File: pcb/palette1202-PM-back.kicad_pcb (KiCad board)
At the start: 2 copper layers, 100 x 86.8 mm, 9 parts

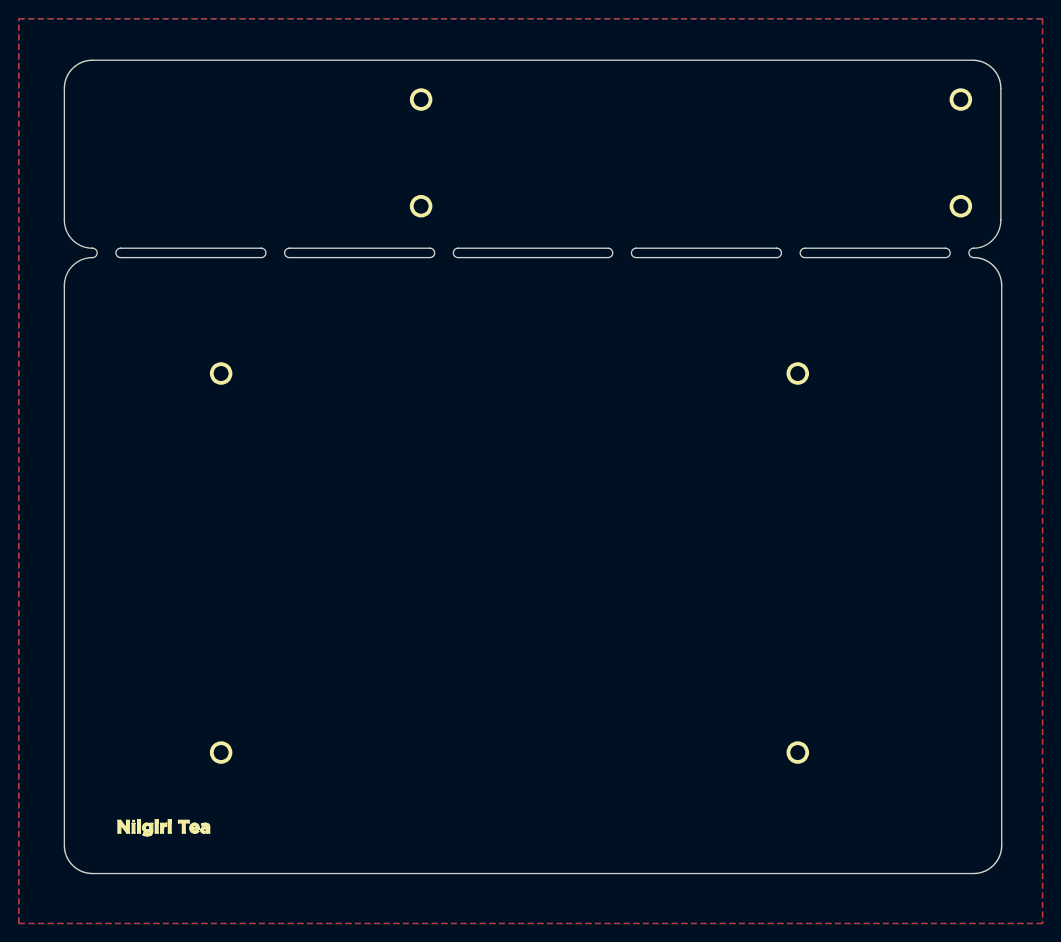
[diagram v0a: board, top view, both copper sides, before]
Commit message: updated back panel
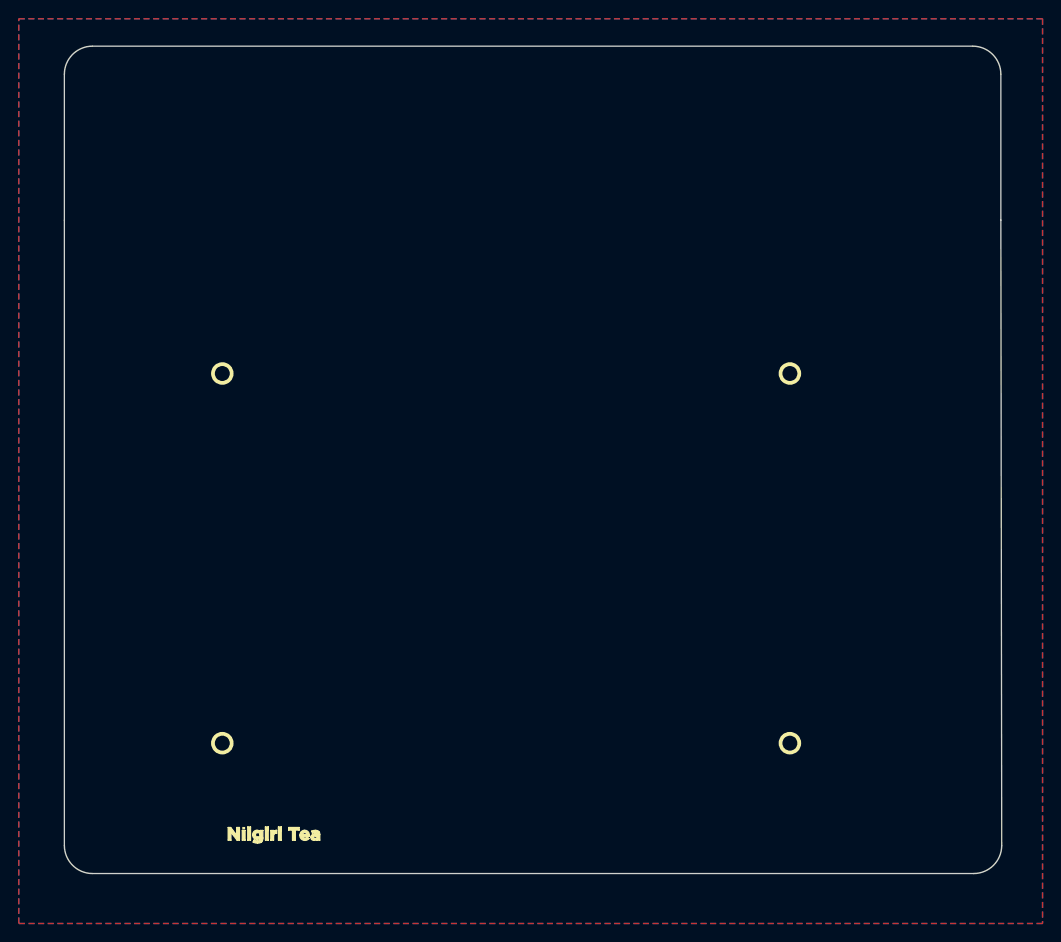
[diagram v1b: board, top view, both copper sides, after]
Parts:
- removed H1, H2, H3, H4: MountingHole, nilgiri:M2_vis
- removed the H99 at (95.1, 119.4)
- added H99: MountingHole, nilgiri:nil_logo, F.Cu at (106.8, 120.1)
- added H99: MountingHole, nilgiri:nil_logo, B.Cu at (108.3, 120.1)
- moved H8 1.31 mm to (163.5, 110.3)
- moved H6 1.01 mm to (103.0, 110.3)
- moved H7 0.84 mm to (163.5, 70.9)
- moved H5 0.13 mm to (103.0, 70.9)
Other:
- board size 100 x 86.8 mm -> 100 x 88.3 mm
- board text removed: "are not correct, except key switches."
- board text removed: "note: the positions or sizes"
- board text removed: "shaft:7mm"
